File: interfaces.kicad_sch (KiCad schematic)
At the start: 116 parts

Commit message: Introduce component standardization
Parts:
- added C134, C136, C192, C193, C241: C_100n_6V3_0402, antmicro-footprints:C_0402_1005Metric, symbol antmicroCapacitorsmisc:C_100n_6V3_0402
- added C190, C191, C45: C_4u7_0603, antmicro-footprints:C_0603_1608Metric, symbol antmicroCapacitors0603:C_4u7_0603
- added R143: R_100R_0402, antmicro-footprints:R_0402_1005Metric, symbol antmicroResistors0402:R_100R_0402
- C10, C107, C11, C12, C13, C135, C139, C149, C169, C170, C172, C173, C174, C18, C19, C20, C21, C22, C24, C248, C249, C25, C251, C252, C253, C254, C26, C4, C5, C6, C7: value (none) -> C_100n_0402; footprint (none) -> antmicro-footprints:C_0402_1005Metric; symbol artix-dc-scm:C_100n_0402 -> antmicroCapacitors0402:C_100n_0402; Author (none) -> Antmicro; Dielectric (none) -> X5R; License (none) -> Apache-2.0; MPN 0402X104K6R3CT -> GRM155R61H104KE14D; Manufacturer Walsin -> Murata; Voltage (none) -> 50V
- C154, C162, C177, C188, C222, C23, C245, C246, C247: value (none) -> C_4u7_0402; footprint (none) -> antmicro-footprints:C_0402_1005Metric; symbol artix-dc-scm:C_4u7_0402 -> antmicroCapacitors0402:C_4u7_0402; Author (none) -> Antmicro; License (none) -> Apache-2.0; Manufacturer MURATA -> Murata
- C166, C168: value (none) -> C_18p_0402; footprint (none) -> antmicro-footprints:C_0402_1005Metric; symbol artix-dc-scm:C_18p_0402 -> antmicroCapacitors0402:C_18p_0402; Author (none) -> Antmicro; License (none) -> Apache-2.0; Manufacturer MULTICOMP -> Multicomp
- C17, C186, C187, C189, C194, C195, C223, C224, C229, C230, C231, C232, C39: value (none) -> C_100n_6V3_0402; footprint (none) -> antmicro-footprints:C_0402_1005Metric; symbol artix-dc-scm:C_100n_0402-artix-dc-scm -> antmicroCapacitorsmisc:C_100n_6V3_0402; Author (none) -> Antmicro; License (none) -> Apache-2.0
- C183, C184, C185: value (none) -> C_2u2_0402; footprint (none) -> antmicro-footprints:C_0402_1005Metric; symbol artix-dc-scm:C_2u2_0402 -> antmicroCapacitors0402:C_2u2_0402; Author (none) -> Antmicro; License (none) -> Apache-2.0
- D15: value (none) -> TPD2E009_SOT-9X3; footprint (none) -> antmicro-footprints:SOT-723; symbol artix-dc-scm:TPD2E009 -> antmicroTVSDiodes:TPD2E009_SOT-9X3; Author (none) -> Antmicro; License (none) -> Apache-2.0
- D2: value (none) -> SP3011-06UTG; footprint (none) -> antmicro-footprints:USON-14_3.5x1.35_P0.5mm; symbol artix-dc-scm:SP3011-06UTG -> antmicroTVSDiodes:SP3011-06UTG; Author (none) -> Antmicro; License (none) -> Apache-2.0
- FB1, FB2: value (none) -> FB_600Z_0.3A_0402; footprint (none) -> antmicro-footprints:FB_0402_1005Metric; symbol artix-dc-scm:BLM15AG601SN1D -> antmicroFerriteBeadsandChips:FB_600Z_0.3A_0402; Author (none) -> Antmicro; License (none) -> Apache-2.0
- J3: value (none) -> USB-Micro-B-10118192-0001LF; footprint (none) -> antmicro-footprints:USB_Micro_B_Female_10118192; symbol artix-dc-scm:10118192-0001LF -> antmicroUSBDVIHDMIConnectors:USB-Micro-B-10118192-0001LF; Author (none) -> Antmicro; License (none) -> Apache-2.0; Manufacturer Amphenol ICC (FCI) -> Amphenol
- J6: value (none) -> 0878311420; footprint (none) -> antmicro-footprints:PinHeader_2x7_P2mm_Drill1mm_Shrouded; symbol artix-dc-scm:0878311420 -> antmicroRectangularConnectorsHeadersMalePins:0878311420; Author (none) -> Antmicro; License (none) -> Apache-2.0
- J7: renamed from J?; value (none) -> 61300611121; footprint (none) -> antmicro-footprints:PinHeader_1x6_P2.54mm; symbol artix-dc-scm:61300611121-artix-dc-scm -> antmicroRectangularConnectorsHeadersMalePins:61300611121; Author (none) -> Antmicro; License (none) -> Apache-2.0; Manufacturer Wurth Electronics Inc. -> Würth Elektronik
- R10, R11: value (none) -> R_0R_0402; footprint (none) -> antmicro-footprints:R_0402_1005Metric; symbol artix-dc-scm:R_0R_0402 -> antmicroResistors0402:R_0R_0402; Author (none) -> Antmicro; Current (none) -> 1A; License (none) -> Apache-2.0; Manufacturer PANASONIC -> Panasonic
- R117, R118, R119, R120, R121, R122, R123, R124, R125, R126: value (none) -> R_47k_0402; footprint (none) -> antmicro-footprints:R_0402_1005Metric; symbol artix-dc-scm:R_47k_0402 -> antmicroResistors0402:R_47k_0402; Author (none) -> Antmicro; License (none) -> Apache-2.0; MPN MCMR04X4702FTL -> CR0402-FX-4702GLF; Manufacturer MULTICOMP -> Bourns; Tolerance (none) -> 1%
- R12, R53, R62: value (none) -> R_200k_0402-artix-dc-scm; footprint (none) -> antmicro-footprints:R_0402_1005Metric; symbol artix-dc-scm:R_200k_0402-artix-dc-scm -> antmicroResistors0402:R_200k_0402; Author (none) -> Antmicro; License (none) -> Apache-2.0; MPN RC0402FR-07200KL -> CR0402-FX-2003GLF; Manufacturer YAGEO_(PHYCOMP) -> Bourns; Tolerance (none) -> 1%
- R160, R191, R192, R193, R195, R196, R9: value (none) -> R_22R_0402; footprint (none) -> antmicro-footprints:R_0402_1005Metric; symbol artix-dc-scm:R_22R_0402 -> antmicroResistors0402:R_22R_0402; Author (none) -> Antmicro; License (none) -> Apache-2.0; MPN CRCW040222R0FKED -> CR0402-FX-22R0GLF; Manufacturer VISHAY -> Bourns; Tolerance (none) -> 1%
- R197: renamed from R?; value (none) -> R_4k7_0402; footprint (none) -> antmicro-footprints:R_0402_1005Metric; symbol artix-dc-scm:R_4k7_0402 -> antmicroResistors0402:R_4k7_0402; Author (none) -> Antmicro; License (none) -> Apache-2.0; MPN ERJ2GEJ472X -> CR0402-FX-4701GLF; Manufacturer PANASONIC_ELECTRONIC_COMPONENTS -> Bourns; Tolerance (none) -> 1%
- R3: value (none) -> R_12k1_0402; footprint (none) -> antmicro-footprints:R_0402_1005Metric; symbol artix-dc-scm:R_12k1_0402 -> antmicroResistors0402:R_12k1_0402; Author (none) -> Antmicro; License (none) -> Apache-2.0; MPN MCWR04X1212FTL -> CR0402-FX-1212GLF; Manufacturer MULTICOMP -> Bourns; Tolerance (none) -> 1%
- R4: value (none) -> R_10k_0402; footprint (none) -> antmicro-footprints:R_0402_1005Metric; symbol artix-dc-scm:R_10k_0402 -> antmicroResistors0402:R_10k_0402; Author (none) -> Antmicro; License (none) -> Apache-2.0; MPN CRCW040210K0FKEDHP -> CR0402-FX-1002GLF; Manufacturer VISHAY -> Bourns; Tolerance (none) -> 1%
- R45, R46, R47, R48, R49, R50, R51, R52: value (none) -> R_357k_0402-artix-dc-scm; footprint (none) -> antmicro-footprints:R_0402_1005Metric; symbol artix-dc-scm:R_357k_0402-artix-dc-scm -> antmicroResistors0402:R_357k_0402; Author (none) -> Antmicro; License (none) -> Apache-2.0; MPN CRCW0402357KFKED -> CR0402-FX-3573GLF; Manufacturer Vishay -> Bourns; Tolerance (none) -> 1%
- R5, R7: value (none) -> R_12k_0402; footprint (none) -> antmicro-footprints:R_0402_1005Metric; symbol artix-dc-scm:R_12k_0402 -> antmicroResistors0402:R_12k_0402; Author (none) -> Antmicro; License (none) -> Apache-2.0; MPN CRCW040212K0FKEDHP -> CR0402-FX-1202GLF; Manufacturer VISHAY -> Bourns; Tolerance (none) -> 1%
- R6, R8: value (none) -> R_1k_0402; footprint (none) -> antmicro-footprints:R_0402_1005Metric; symbol artix-dc-scm:R_1k_0402 -> antmicroResistors0402:R_1k_0402; Author (none) -> Antmicro; License (none) -> Apache-2.0; Manufacturer BOURNS -> Bourns; Tolerance (none) -> 1%
- TP3: value (none) -> TP_SMD1MM; footprint (none) -> antmicro-footprints:Testpoint_smd_1mm; symbol artix-dc-scm:TP_SMD1MM -> antmicroTestPoints:TP_1mm_SMD; Author (none) -> Antmicro; DNP (none) -> DNP; License (none) -> Apache-2.0
- TP7, TP8: renamed from TP?; value (none) -> TP_SMD1MM; footprint (none) -> antmicro-footprints:Testpoint_smd_1mm; symbol artix-dc-scm:TP_SMD1MM -> antmicroTestPoints:TP_1mm_SMD; Author (none) -> Antmicro; DNP (none) -> DNP; License (none) -> Apache-2.0
- U1: value (none) -> MTFC16GAPALNA-AIT; footprint (none) -> antmicro-footprints:BGA-100_18x14mm_Layout17x10_P1mm; symbol artix-dc-scm:MTFC16GAPALNA-AIT -> antmicroMemory:MTFC16GAPALNA-AIT; Author (none) -> Antmicro; License (none) -> Apache-2.0; MANUFACTURER Micron -> (none); MPN (none) -> MTFC16GAPALNA-AIT; Manufacturer (none) -> Micron; Package 100-ball TBGA 14x18 -> (none)
- U14: value (none) -> XC7A100T-FGG484; footprint (none) -> antmicro-footprints:BGA-484_23x23mm_Layout22x22_P1mm_Xilinx_FGG484; symbol artix-dc-scm:XC7A100T-FGG484 -> antmicroMicrocontrollers:XC7A100T-FGG484; Author (none) -> Antmicro; License (none) -> Apache-2.0; MPN (none) -> XC7A100T-FGG484; Manufacturer (none) -> Xilinx
- U17, U18: value (none) -> USB3300-EZK-TR; footprint (none) -> antmicro-footprints:QFN-32-1EP_5x5mm; symbol artix-dc-scm:USB3300-EZK-TR -> antmicroInterfaceControllers:USB3300-EZK-TR; Author (none) -> Antmicro; License (none) -> Apache-2.0
- U19: value (none) -> FT4232H_QFN; footprint (none) -> antmicro-footprints:QFN-64_1EP_9x9mm_P0.5mm; symbol artix-dc-scm:FT4232HQ -> antmicroInterfaceControllers:FT4232H_QFN; Author (none) -> Antmicro; License (none) -> Apache-2.0
- U21: value (none) -> LSF0108RKSR; footprint (none) -> antmicro-footprints:VQFN-20_1EP_4.5x2.5mm_P0.5mm; symbol artix-dc-scm:LSF0108RKSR -> antmicroLogicTranslatorsLevelShifters:LSF0108RKSR; Author (none) -> Antmicro; License (none) -> Apache-2.0; MANUFACTURER Texas Instruments -> (none); MPN (none) -> LSF0108RKSR; Manufacturer (none) -> Texas Instruments
- U22: value (none) -> LSF0101DRYR; footprint (none) -> antmicro-footprints:USON-6_1.45x1.0mm_P0.5mm_Texas_DRY6; symbol artix-dc-scm:LSF0101DRYR -> antmicroLogicTranslatorsLevelShifters:LSF0101DRYR; Author (none) -> Antmicro; License (none) -> Apache-2.0; MPN (none) -> LSF0101DRYR; Manufacturer (none) -> Texas Instruments
- U23, U24: value (none) -> ASEMB-24.000MHZ-LC-T; footprint (none) -> antmicro-footprints:Oscillator_SMD_Abracon_ASEM_3.2x2.5mm; symbol artix-dc-scm:ASEMB-24.000MHZ-LC-T -> antmicroOscillators:Oscillator_SMD_24MHz_ASEMB; Author (none) -> Antmicro; License (none) -> Apache-2.0; MPN (none) -> ASEMB-24.000MHZ-LC-T; Manufacturer (none) -> Abracon; Val (none) -> 24MHz
- U6: value (none) -> NVT2008BQ,115; footprint (none) -> antmicro-footprints:VQFN-20_1EP_4.5x2.5mm_P0.5mm; symbol artix-dc-scm:NVT2008DQ,115-artix-dc-scm -> antmicroLogicTranslatorsLevelShifters:NVT2008BQ,115; Author (none) -> Antmicro; License (none) -> Apache-2.0; Manufacturer NXP Semiconductors -> NXP
- Y1: value (none) -> Oscillator_SMD_12MHz_KX-7; footprint (none) -> antmicro-footprints:Oscillator_SMD_Geyer_KX-7-4Pin_3.2x2.5mm; symbol artix-dc-scm:ABM8G-12.000MHZ-18-D2Y-T -> antmicroCrystals:Oscillator_SMD_12MHz_KX-7; Author (none) -> Antmicro; License (none) -> Apache-2.0; Val (none) -> 12MHz
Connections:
- net 1V8_FT: now also C107.2, C135.2, C6.2, C7.2; no longer C107.1, C135.1, C6.1, C7.1
- net FT_VPHY: now also C139.2, C162.2; no longer C139.1, C162.1
- net FT_VPLL: now also C149.2, C154.2; no longer C149.1, C154.1
- net GND: now also C10.1, C107.1, C11.1, C12.1, C13.1, C135.1, C139.1, C149.1, C154.1, C162.1, C166.1, C168.1, C169.1, C170.1, C172.1, C173.1, C174.1, C177.1, C18.1, C183.1, C184.1, C185.1, C186.1, C187.1, C188.1, C189.1, C19.1, C20.1, C21.1, C22.1, C222.1, C223.1, C224.1, C229.1, C23.1, C230.1, C231.1, C232.1, C24.1, C245.1, C246.1, C247.1, C248.1, C249.1, C25.1, C251.1, C252.1, C253.1, C254.1, C26.1, C4.1, C6.1, C7.1, D2.5, U6.21 (EP), C134.1, C136.1, C190.1, C191.1, C192.1, C193.1, C241.1, C45.1; no longer C10.2, C107.2, C11.2, C12.2, C13.2, C135.2, C139.2, C149.2, C154.2, C162.2, C166.2, C168.2, C169.2, C170.2, C172.2, C173.2, C174.2, C177.2, C18.2, C183.2, C184.2, C185.2, C186.2, C187.2, C188.2, C189.2, C19.2, C20.2, C21.2, C22.2, C222.2, C223.2, C224.2, C229.2, C23.2, C230.2, C231.2, C232.2, C24.2, C245.2, C246.2, C247.2, C248.2, C249.2, C25.2, C251.2, C252.2, C253.2, C254.2, C26.2, C4.2, C6.2, C7.2
- net JTAG_TCK: now also D2.2
- net JTAG_TDI: now also D2.7
- net JTAG_TDO: now also D2.6
- net JTAG_TMS: now also D2.1
- net PCIE_BMC_TX_C_N: now also C194.2; no longer C194.1
- net PCIE_BMC_TX_C_P: now also C195.2; no longer C195.1
- net PCIE_BMC_TX_N: now also C194.1; no longer C194.2
- net PCIE_BMC_TX_P: now also C195.1; no longer C195.2
- net VCC1V0: now also U14.D10 (MGTAVCC), U14.D6 (MGTAVCC), U14.E8 (MGTAVCC), U14.F7 (MGTAVCC), U14.F9 (MGTAVCC), C134.2, C136.2, C190.2
- net VCC1V8: now also C253.2, C254.2; no longer C253.1, C254.1
- net VCC3V3: now also C10.2, C11.2, C12.2, C13.2, C169.2, C170.2, C172.2, C173.2, C174.2, C18.2, C183.2, C184.2, C185.2, C186.2, C187.2, C19.2, C21.2, C222.2, C223.2, C224.2, C229.2, C23.2, C230.2, C231.2, C232.2, C24.2, C251.2, C252.2, C4.2, R10.1, R12.2, R62.2; no longer C10.1, C11.1, C12.1, C13.1, C169.1, C170.1, C172.1, C173.1, C174.1, C18.1, C183.1, C184.1, C185.1, C186.1, C187.1, C19.1, C21.1, C222.1, C223.1, C224.1, C229.1, C23.1, C230.1, C231.1, C232.1, C24.1, C251.1, C252.1, C4.1, R10.2, R12.1, R62.1
- net at U17.31 (REG_EN): now also R10.2; no longer R10.1
- net at U21.20 (EN): now also R12.1; no longer R12.2
- net at U22.6 (EN): now also R62.1; no longer R62.2
- net at D2.11: now also D2.4
- net at D2.12: now also D2.3
- net at U19.2 (OSCI), Y1.1: now also C166.2; no longer C166.1
- net at U19.3 (OSCO), Y1.3: now also C168.2; no longer C168.1
- new net: C20.2, C247.2, C249.2, U17.15 (VDD1.8), U17.26 (VDD1.8)
- new net: C246.2, C25.2, U17.29 (VDDA1.8)
- new net: C188.2, C189.2, U1.E4 (VDDIM)
- new net: C22.2, C245.2, U18.29 (VDDA1.8)
- new net: C177.2, C248.2, C26.2, U18.15 (VDD1.8), U18.26 (VDD1.8)
- new net: R143.1, U14.F8 (MGTRREF_216)
- new net VCC1V2: C191.2, C192.2, C193.2, C241.2, C45.2, R143.2, U14.B11 (MGTAVTT), U14.B5 (MGTAVTT), U14.B7 (MGTAVTT), U14.B9 (MGTAVTT), U14.C4 (MGTAVTT), U14.C8 (MGTAVTT)
- no-connect marks 13 -> 56
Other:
- note added: "Pull up via 10KOhm"
- note added: "Transceiver supply"
- moved on the sheet: C10, C107, C11, C12, C13, C135, C139, C149, C154, C162, C166, C168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

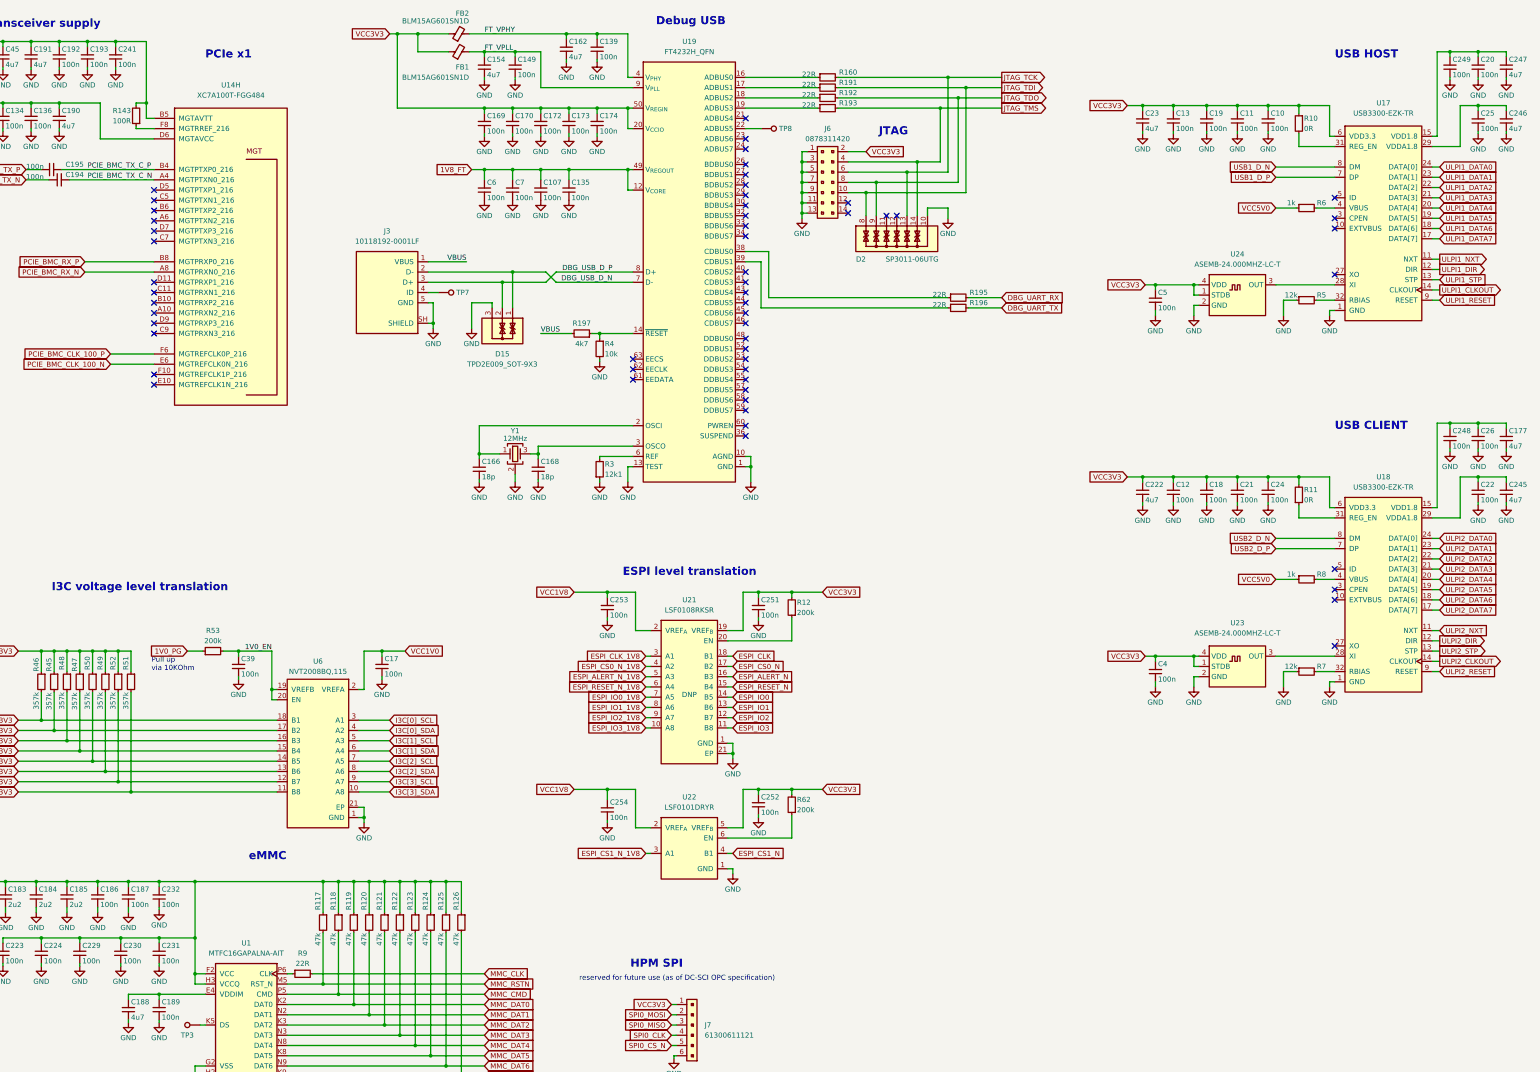
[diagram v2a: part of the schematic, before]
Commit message: Fix schematic ERC errors. ERC clean
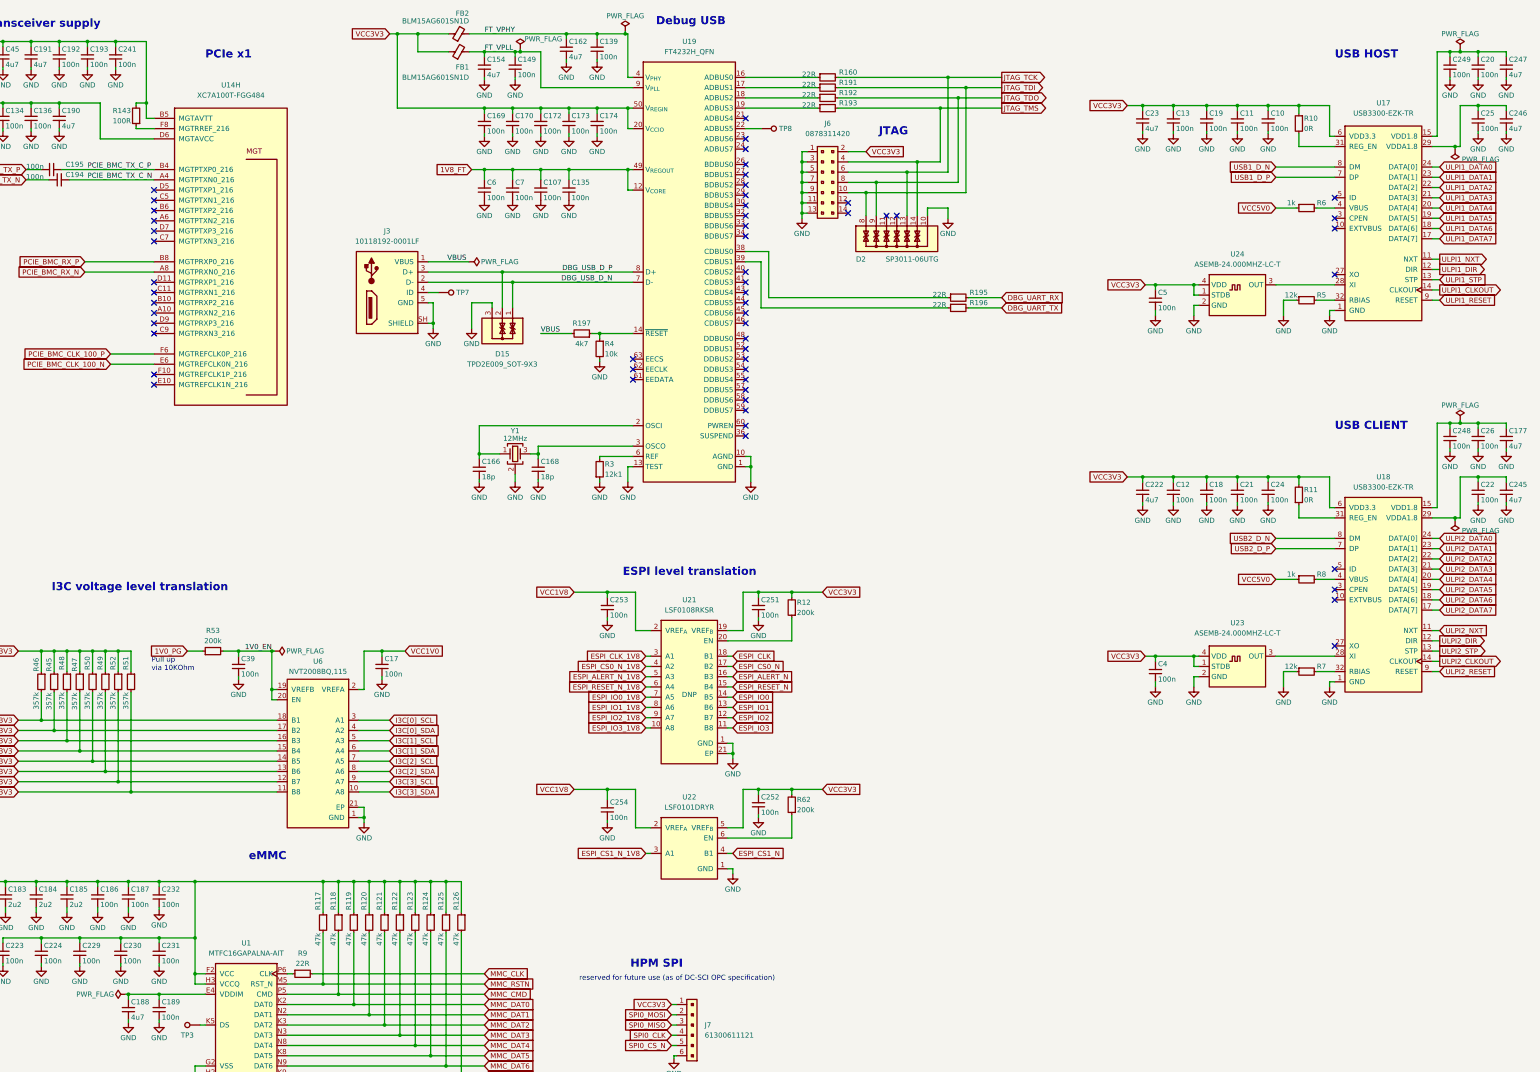
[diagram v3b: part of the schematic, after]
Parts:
- J6: symbol antmicroRectangularConnectorsHeadersMalePins:0878311420 -> antmicroRectangularConnectorsHeadersMalePins:PinHeader_2x7_P2mm_Drill1mm_Shrouded
